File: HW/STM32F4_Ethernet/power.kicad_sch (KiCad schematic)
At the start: 4 parts

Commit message: Progress backup. add SRAM
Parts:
- added FB5: MPZ1608S601A, BEADC1608X95N, symbol MPZ1608S601A:MPZ1608S601A
- added U5: DCP012415DBP-U, SOP254P1050X533-14N, symbol DCP012415DBP-U:DCP012415DBP-U
- gave numbers to parts that had none: 4
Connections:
- net GND: now also U5.5 (0V)
- net USB_POWER: now also FB5.2
- new net +5V: FB5.1, U5.6 (+VOUT)
- new net ISO_+24V: U5.1 (VS)
- new net ISO_GND: U5.2 (0V_2)
- no-connect marks 0 -> 3
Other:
- moved on the sheet: C51, C52, C53, U6

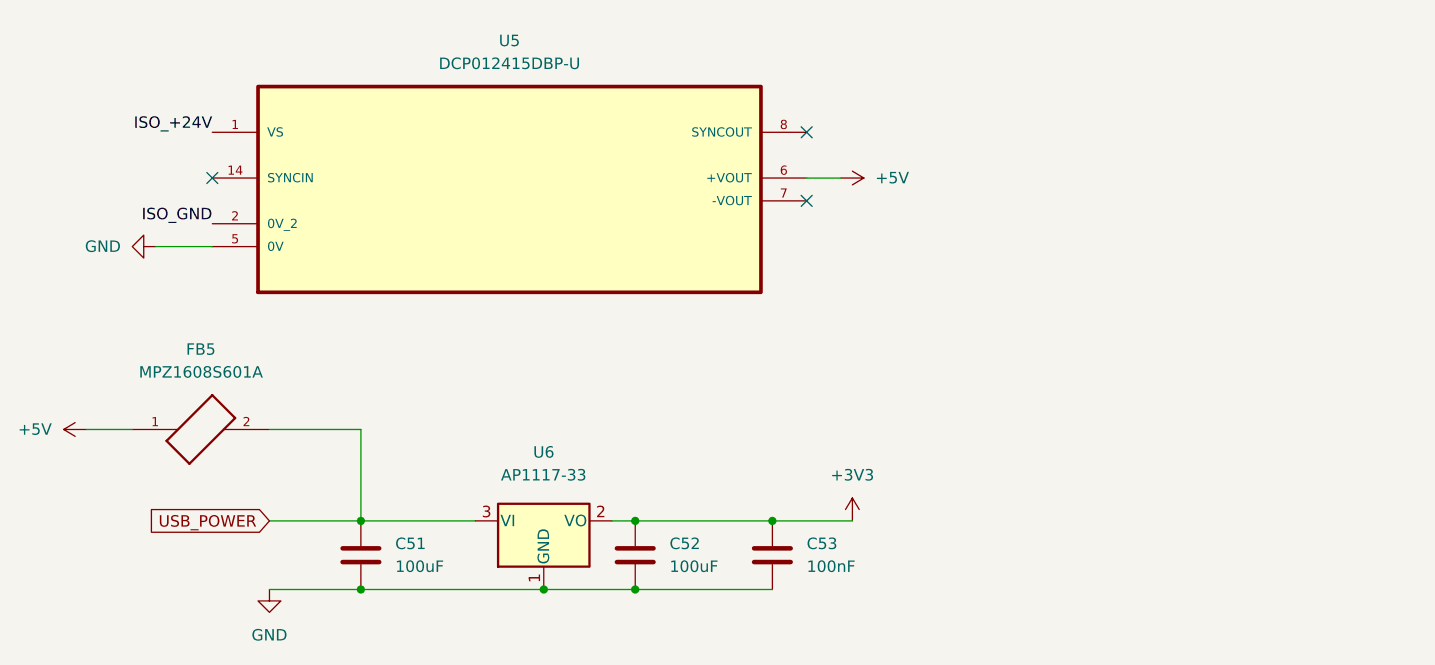
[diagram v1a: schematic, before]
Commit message: Sample PCB. Need to update RLC Size
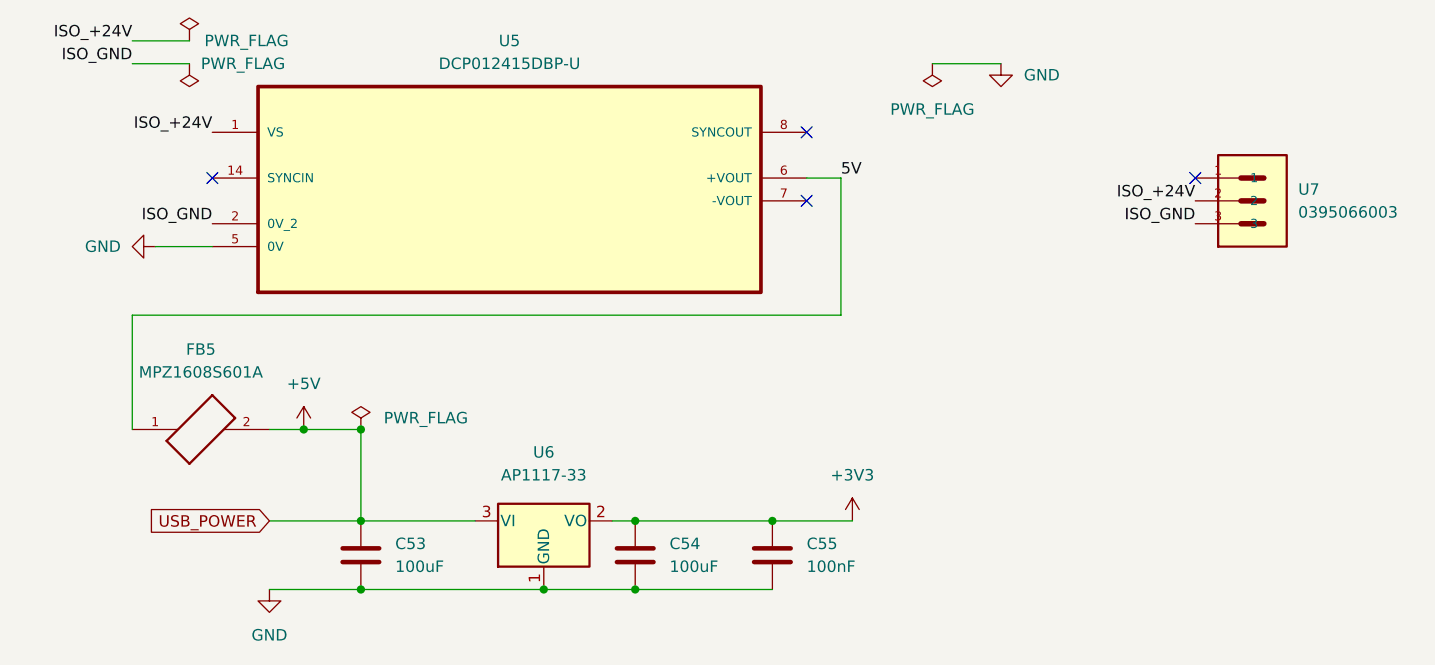
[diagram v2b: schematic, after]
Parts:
- added U7: 0395066003, MOLEX_0395066003, symbol 0395066003:0395066003
- C53: renamed from C51; footprint (none) -> Capacitor_SMD:C_0603_1608Metric_Pad1.08x0.95mm_HandSolder
- C54: renamed from C52; footprint (none) -> Capacitor_SMD:C_0603_1608Metric_Pad1.08x0.95mm_HandSolder
- C55: renamed from C53; footprint (none) -> Capacitor_SMD:C_0603_1608Metric_Pad1.08x0.95mm_HandSolder
- FB5: footprint BEADC1608X95N -> MPZ1608S601A:BEADC1608X95N
- U5: footprint SOP254P1050X533-14N -> DCP012415DBP-U:SOP254P1050X533-14N
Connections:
- net USB_POWER is gone; now on net +5V: C53.1, FB5.2, U6.3 (VI)
- net +5V: no longer FB5.1, U5.6 (+VOUT)
- net ISO_+24V: now also U7.2
- net ISO_GND: now also U7.3
- new net 5V: FB5.1, U5.6 (+VOUT)
- no-connect marks 3 -> 4
